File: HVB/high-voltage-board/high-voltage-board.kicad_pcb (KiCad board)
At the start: 2 copper layers, 66 parts, among them J1 Conn_01x23, J10 Conn_01x05, J2 HECS, J3 HV+, J4 HV-, J5 HV+, J6 HV-, J7 Conn_01x02, J9 Bender-LV, Q1 040N03LG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

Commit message: working on layout
Updating traces for RCB and organizing HVB
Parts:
- removed R13: 10k, Resistor_SMD:R_0603_1608Metric_Pad0.98x0.95mm_HandSolder
- C11, C18, C7, R11, R14, R16, R17, R18, R19, R2, U2, U6, U8, U9: moved to B.Cu
- moved R11 135.3 mm to (141.2, 108.7), turned to -90 degrees
- moved R6 133.7 mm to (136.1, 50.3)
- moved C14 128.4 mm to (144.8, 83.3)
- moved Q2 128.2 mm to (147.3, 59.9)
- moved C18 124.4 mm to (145.4, 104.6)
- moved C10 123.6 mm to (145.8, 74.8), turned to 90 degrees
- moved J2 121.4 mm to (68.1, 123.1), turned to 90 degrees
- moved J9 118.0 mm to (78.0, 113.1), turned to -90 degrees
- moved R14 117.2 mm to (145.4, 110.7)
- moved C13 117.0 mm to (144.8, 81.3)
- moved C7 115.9 mm to (143.8, 95.0), turned to -90 degrees
- moved C17 115.8 mm to (149.9, 69.6), turned to 90 degrees
- moved C11 114.6 mm to (143.8, 91.1), turned to 90 degrees
- moved R8 112.2 mm to (144.8, 79.2), turned to 180 degrees
- moved C16 111.6 mm to (151.9, 69.6), turned to 90 degrees
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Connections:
- net /HV+ renamed HV+
- net /HV- renamed HV-
- J1 pad 21: unconnected-(J1-Pad21) -> +5VA
- J1 pad 22: +5V -> unconnected-(J1-Pad22)
- J1 pad 9: /FANOUT2 -> /DCDC_OUT
- J10 pad 1: +3V3 -> A13_SWDIO
- J10 pad 2: A13_SWDIO -> A14_SWCLK
- J10 pad 3: A14_SWCLK -> B3_TRACESWO
- J10 pad 4: B3_TRACESWO -> +3V3
- J2 pad 2: +5V -> +5VA
- J7 pad 1: /TEMP_2 -> /TEMP-
- J7 pad 2: /TEMP_1 -> +3V3
- R12 pad 2: /TEMP_1 -> /TEMP-
- R19 pad 2: +5V -> +3V3
- U5 pad 10: /DC_DC_TRIM_EN -> unconnected-(U5-Pad10)
- U5 pad 13: /TEMP_1 -> unconnected-(U5-Pad13)
- U5 pad 14: /TEMP_2 -> unconnected-(U5-Pad14)
- U5 pad 16: /DC_DC_EN -> unconnected-(U5-Pad16)
- U5 pad 2: /controller/LED1 -> unconnected-(U5-Pad2)
- U5 pad 29: /DC_DC_FAULT -> unconnected-(U5-Pad29)
- U5 pad 3: /controller/LED2 -> unconnected-(U5-Pad3)
- U5 pad 41: unconnected-(U5-Pad41) -> /TEMP-
- U5 pad 42: unconnected-(U5-Pad42) -> /DC_DC_FAULT
- U5 pad 43: unconnected-(U5-Pad43) -> /DC_DC_EN
- U5 pad 45: unconnected-(U5-Pad45) -> /DC_DC_TRIM_EN

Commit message: updating trace layout
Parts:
- moved R1 25.4 mm to (88.9, 53.3), turned to 0 degrees
- moved L1 8.87 mm to (47.8, 57.4), turned to -90 degrees
- moved J5 7.73 mm to (29.8, 43.2)
- moved J3 5.08 mm to (32.5, 73.2)
- moved J4 5.08 mm to (33.0, 93.0)
- moved J6 4.02 mm to (41.7, 105.8)
- moved R15 2.73 mm to (41.1, 57.4), turned to 90 degrees
- moved RV1 2.59 mm to (65.0, 55.4)
- moved C15 1.27 mm to (153.9, 68.3)
- moved C16 1.27 mm to (151.9, 68.3)
- moved C17 1.27 mm to (149.9, 68.3)
- moved C8 1.27 mm to (151.7, 127.8)
- moved C9 1.27 mm to (147.8, 127.8)
- moved D1 1.27 mm to (150.9, 124.5)
- moved D2 1.27 mm to (157.0, 121.7)
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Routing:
- net HV+: track 0.00 -> 125.7 mm
- net /vicor/HV+: track 0.00 -> 29.2 mm
- net /TSAL/HV+: track 0.00 -> 8.96 mm
- net Net-(C19-Pad1): track 0.00 -> 6.83 mm
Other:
- board outline added: 135.9 x 96.5 mm

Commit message: adding traces
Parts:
- R16: moved to F.Cu
- moved R16 12.8 mm to (67.6, 62.2), turned to 0 degrees
- moved RV1 6.76 mm to (59.1, 52.1), turned to -90 degrees
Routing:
- net HV-: track 0.00 -> 42.0 mm
- net /vicor/TRIM_HV: track 0.00 -> 37.4 mm
- added copper zone on B.Cu, net HV-
- added copper zone on F.Cu, net HV-
- added copper zone on F.Cu, net Net-(C19-Pad1)

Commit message: updating hv layout
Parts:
- moved R2 6.72 mm to (100.6, 72.1)
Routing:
- net HV-: track 42.0 -> 106.1 mm
- net Net-(R1-Pad1): track 0.00 -> 30.5 mm
- net /vicor/FAULT_HV: track 0.00 -> 27.0 mm
- net /vicor/EN_HV: track 0.00 -> 22.9 mm
- net /DC_DC_FAULT: track 0.00 -> 3.98 mm
- net Net-(R18-Pad2): track 0.00 -> 3.91 mm
- net Net-(R17-Pad1): track 0.00 -> 3.05 mm
- added copper zone on B.Cu, net Net-(C19-Pad1)
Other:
- outline, holes or cut-outs redrawn
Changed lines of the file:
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@@
   )
   (footprint "Resistor_SMD:R_0603_1608Metric_Pad0.98x0.95mm_HandSolder" (layer "B.Cu")
-    (at 94.5915 69.088)
+    (at 100.584 72.136)
     (descr "Resistor SMD 0603 (1608 Metric), square (rectangular) end terminal, IPC_7351 nominal with elongated pad for handsoldering. (Body size source: IPC-SM-782 page 72, https://www.pcb-3d.com/wordpress/wp-content/uploads/ipc-sm-782a_amendment_1_and_2.pdf), generated with kicad-footprint-generator")
     (tags "resistor handsolder")
@@
   )
   (gr_line (start 161.29 129.54) (end 160.02 129.54) (layer "Edge.Cuts") (width 0.1))
+  (gr_line (start 90.932 104.14) (end 90.932 103.124) (layer "Edge.Cuts") (width 0.1))
+  (gr_arc (start 117.856 39.624) (mid 120.904 36.576) (end 123.952 39.624) (layer "Edge.Cuts") (width 0.1))
+  (gr_line (start 92.456 90.424) (end 90.932 94.488) (layer "Edge.Cuts") (width 0.1))
+  (gr_line (start 92.456 70.612) (end 92.456 68.58) (layer "Edge.Cuts") (width 0.1))
+  (gr_line (start 92.456 85.852) (end 92.456 90.424) (layer "Edge.Cuts") (width 0.1))
+  (gr_line (start 117.856 56.388) (end 117.856 39.624) (layer "Edge.Cuts") (width 0.1))
+  (gr_line (start 87.884 99.568) (end 87.884 104.14) (layer "Edge.Cuts") (width 0.1))
   (gr_line (start 25.4 33.02) (end 158.75 33.02) (layer "Edge.Cuts") (width 0.1))
   (gr_line (start 25.4 38.1) (end 25.4 129.54) (layer "Edge.Cuts") (width 0.1))
+  (gr_arc (start 123.952 62.484) (mid 120.904 65.532) (end 117.856 62.484) (layer "Edge.Cuts") (width 0.1))
+  (gr_arc (start 87.884 67.056) (mid 90.17 64.77) (end 92.456 67.056) (layer "Edge.Cuts") (width 0.1))
+  (gr_line (start 90.932 94.488) (end 90.932 103.124) (layer "Edge.Cuts") (width 0.1))
   (gr_line (start 158.75 33.02) (end 161.29 33.02) (layer "Edge.Cuts") (width 0.1))
   (gr_line (start 25.4 38.1) (end 25.4 33.02) (layer "Edge.Cuts") (width 0.1))
+  (gr_line (start 92.456 67.056) (end 92.456 68.58) (layer "Edge.Cuts") (width 0.1))
   (gr_line (start 161.29 33.02) (end 161.29 129.54) (layer "Edge.Cuts") (width 0.1))
+  (gr_arc (start 90.932 104.14) (mid 89.408 105.664) (end 87.884 104.14) (layer "Edge.Cuts") (width 0.1))
+  (gr_line (start 87.884 67.056) (end 87.884 68.58) (layer "Edge.Cuts") (width 0.1))
+  (gr_line (start 117.856 56.388) (end 117.856 62.484) (layer "Edge.Cuts") (width 0.1))
+  (gr_line (start 87.884 99.568) (end 87.884 68.58) (layer "Edge.Cuts") (width 0.1))
+  (gr_line (start 123.952 39.624) (end 123.952 62.484) (layer "Edge.Cuts") (width 0.1))
   (gr_line (start 25.4 129.54) (end 160.02 129.54) (layer "Edge.Cuts") (width 0.1))
+  (gr_line (start 92.456 70.612) (end 92.456 85.852) (layer "Edge.Cuts") (width 0.1))
+  (dimension (type aligned) (layer "B.SilkS")
+    (pts (xy 87.884 67.056) (xy 92.456 67.056))
+    (height -3.556)
+    (gr_text "4.5720 mm" (at 90.17 62.35) (layer "B.SilkS")
+      (effects (font (size 1 1) (thickness 0.15)))
+    )
+    (format (units 3) (units_format 1) (precision 4))
+    (style (thickness 0.15) (arrow_length 1.27) (text_position_mode 0) (extension_height 0.58642) (extension_offset 0.5) keep_text_aligned)
+  )
+  (dimension (type aligned) (layer "F.SilkS")
+    (pts (xy 117.856 39.624) (xy 123.952 39.624))
+    (height -4.064)
+    (gr_text "6.0960 mm" (at 120.904 34.41) (layer "F.SilkS")
+      (effects (font (size 1 1) (thickness 0.15)))
+    )
+    (format (units 3) (units_format 1) (precision 4))
+    (style (thickness 0.15) (arrow_length 1.27) (text_position_mode 0) (extension_height 0.58642) (extension_offset 0.5) keep_text_aligned)
+  )
   (dimension (type aligned) (layer "Dwgs.User")
     (pts (xy 22.86 137.16) (xy 22.445 36.83))
@@
   (segment (start 41.148 60.454) (end 47.202 60.454) (width 3.6) (layer "F.Cu") (net 12))
   (segment (start 47.202 60.454) (end 47.752 59.904) (width 3.6) (layer "F.Cu") (net 12))
+  (segment (start 85.852 53.34) (end 88.9 53.34) (width 0.36) (layer "B.Cu") (net 30))
+  (segment (start 81.534 74.93) (end 79.756 73.152) (width 0.36) (layer "B.Cu") (net 30))
+  (segment (start 79.756 73.152) (end 79.756 59.436) (width 0.36) (layer "B.Cu") (net 30))
+  (segment (start 84.135 74.93) (end 81.534 74.93) (width 0.36) (layer "B.Cu") (net 30))
+  (segment (start 79.756 59.436) (end 85.852 53.34) (width 0.36) (layer "B.Cu") (net 30))
+  (segment (start 85.75 97.79) (end 83.058 97.79) (width 0.36) (layer "B.Cu") (net 35))
+  (segment (start 83.058 97.79) (end 82.804 97.536) (width 0.36) (layer "B.Cu") (net 35))
+  (segment (start 82.804 99.361) (end 76.91322 99.361) (width 0.36) (layer "B.Cu") (net 36))
+  (segment (start 76.91322 99.361) (end 62.00512 84.4529) (width 0.36) (layer "B.Cu") (net 36))
+  (segment (start 97.536 83.7165) (end 97.4325 83.82) (width 0.36) (layer "B.Cu") (net 38))
+  (segment (start 97.4325 83.82) (end 93.665 83.82) (width 0.36) (layer "B.Cu") (net 38))
+  (segment (start 95.965 97.79) (end 96.012 97.743) (width 0.36) (layer "B.Cu") (net 39))
+  (segment (start 92.05 97.79) (end 95.965 97.79) (width 0.36) (layer "B.Cu") (net 39))
   (segment (start 68.025 52.15) (end 71.12 55.245) (width 0.36) (layer "F.Cu") (net 41))
   (segment (start 71.12 55.245) (end 71.12 72.39) (width 0.36) (layer "F.Cu") (net 41))
@@
   (segment (start 64.12 52.15) (end 68.025 52.15) (width 0.36) (layer "F.Cu") (net 41))
   (segment (start 64.1329 79.3729) (end 62.00512 79.3729) (width 0.36) (layer "F.Cu") (net 41))
+  (segment (start 84.135 83.82) (end 80.772 83.82) (width 0.36) (layer "B.Cu") (net 66))
+  (segment (start 78.8649 81.9129) (end 62.00512 81.9129) (width 0.36) (layer "B.Cu") (net 66))
+  (segment (start 80.772 83.82) (end 78.8649 81.9129) (width 0.36) (layer "B.Cu") (net 66))
   (segment (start 58.42 76.835) (end 57.15 78.105) (width 0.36) (layer "F.Cu") (net 67))
   (segment (start 57.15 90.72806) (end 61.03484 94.6129) (width 0.36) (layer "F.Cu") (net 67))
@@
   (segment (start 68.5 62.23) (end 68.5 72.47) (width 0.36) (layer "F.Cu") (net 67))
   (segment (start 64.135 76.835) (end 58.42 76.835) (width 0.36) (layer "F.Cu") (net 67))
+  (segment (start 72.644 101.092) (end 66.1649 94.6129) (width 0.36) (layer "B.Cu") (net 67))
+  (segment (start 86.36 94.996) (end 86.36 89.916) (width 0.36) (layer "B.Cu") (net 67))
+  (segment (start 86.36 89.916) (end 86.36 73.66) (width 0.36) (layer "B.Cu") (net 67))
+  (segment (start 84.135 87.691) (end 86.36 89.916) (width 0.36) (layer "B.Cu") (net 67))
+  (segment (start 87.376 99.568) (end 85.852 101.092) (width 0.36) (layer "B.Cu") (net 67))
+  (segment (start 87.376 96.012) (end 87.376 99.568) (width 0.36) (layer "B.Cu") (net 67))
+  (segment (start 87.376 96.012) (end 86.614 95.25) (width 0.36) (layer "B.Cu") (net 67))
+  (segment (start 86.36 73.66) (end 85.09 72.39) (width 0.36) (layer "B.Cu") (net 67))
+  (segment (start 85.75 95.25) (end 86.614 95.25) (width 0.36) (layer "B.Cu") (net 67))
+  (segment (start 85.852 101.092) (end 72.644 101.092) (width 0.36) (layer "B.Cu") (net 67))
+  (segment (start 85.09 72.39) (end 84.135 72.39) (width 0.36) (layer "B.Cu") (net 67))
+  (segment (start 84.135 86.36) (end 84.135 87.691) (width 0.36) (layer "B.Cu") (net 67))
+  (segment (start 66.1649 94.6129) (end 61.03484 94.6129) (width 0.36) (layer "B.Cu") (net 67))
+  (segment (start 86.614 95.25) (end 86.36 94.996) (width 0.36) (layer "B.Cu") (net 67))
   (segment (start 29.82 43.18) (end 29.82 70.46) (width 3.6) (layer "F.Cu") (net 68))
   (segment (start 91.62 38.81952) (end 91.62 44.45) (width 3.6) (layer "F.Cu") (net 68))
@@
   (segment (start 41.698 54.904) (end 41.148 54.354) (width 3.6) (layer "F.Cu") (net 74))
   (segment (start 47.752 54.904) (end 41.698 54.904) (width 3.6) (layer "F.Cu") (net 74))
-  (zone (net 12) (net_name "Net-(C19-Pad1)") (layer "F.Cu") (hatch edge 0.508)
+  (zone (net 12) (net_name "Net-(C19-Pad1)") (layers F&B.Cu) (hatch edge 0.508)
     (priority 1)
     (connect_pads (clearance 0.508))

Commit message: working on layout
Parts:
- moved J9 9.91 mm to (68.1, 113.4)
- moved J2 8.66 mm to (76.7, 123.4)
- moved D1 1.55 mm to (149.4, 124.2), turned to 180 degrees
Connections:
- D1 pad 2: VDD -> +12V
- J1 pad 1: +12V -> /DCDC_OUT
- J1 pad 10: +12V -> +5VA
- J1 pad 11: GND -> unconnected-(J1-Pad11)
- J1 pad 12: /CAN- -> GND
- J1 pad 13: /CAN+ -> +12V
- J1 pad 14: /DCDC_OUT -> /CAN+
- J1 pad 15: /CAN- -> /CAN+
- J1 pad 16: /CAN+ -> /HECS_AN1
- J1 pad 18: /HECS_AN2 -> /IMD_OK
- J1 pad 19: /HECS_AN1 -> unconnected-(J1-Pad19)
- J1 pad 2: /TSAL_GND -> /DCDC_OUT
- J1 pad 20: /IMD_OK -> +12V
- J1 pad 21: +5VA -> GND
- J1 pad 22: unconnected-(J1-Pad22) -> /CAN-
- J1 pad 23: unconnected-(J1-Pad23) -> /CAN-
- J1 pad 3: +12V -> /DCDC_OUT
- J1 pad 4: GND -> /DCDC_OUT
- J1 pad 6: GND -> +12V
- J1 pad 7: /DCDC_OUT -> +12V
- J1 pad 8: /DCDC_OUT -> /TSAL_GND
- J1 pad 9: /DCDC_OUT -> /HECS_AN2
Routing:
- net +12V: track 0.00 -> 101.4 mm
- net /IMD_OK: track 0.00 -> 44.0 mm
- net +5VA: track 0.00 -> 36.9 mm
- net /HECS_AN2: track 0.00 -> 33.8 mm
- net /HECS_AN3: track 0.00 -> 31.6 mm
- net /HECS_AN1: track 0.00 -> 26.4 mm
- added copper zone on B.Cu, net GND
- added copper zone on F.Cu, net GND

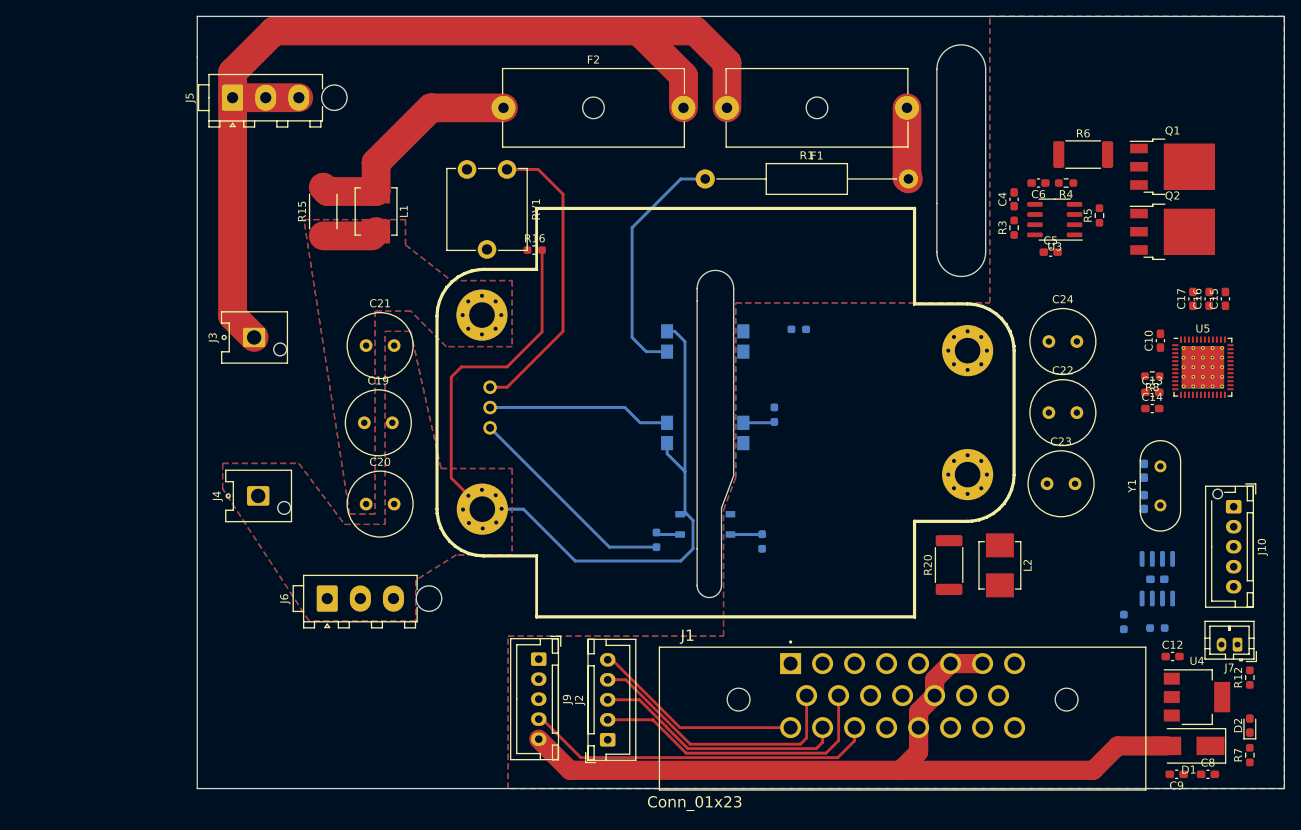
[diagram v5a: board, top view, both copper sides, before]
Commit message: almost done with layout
HV layout almost done. Tracing
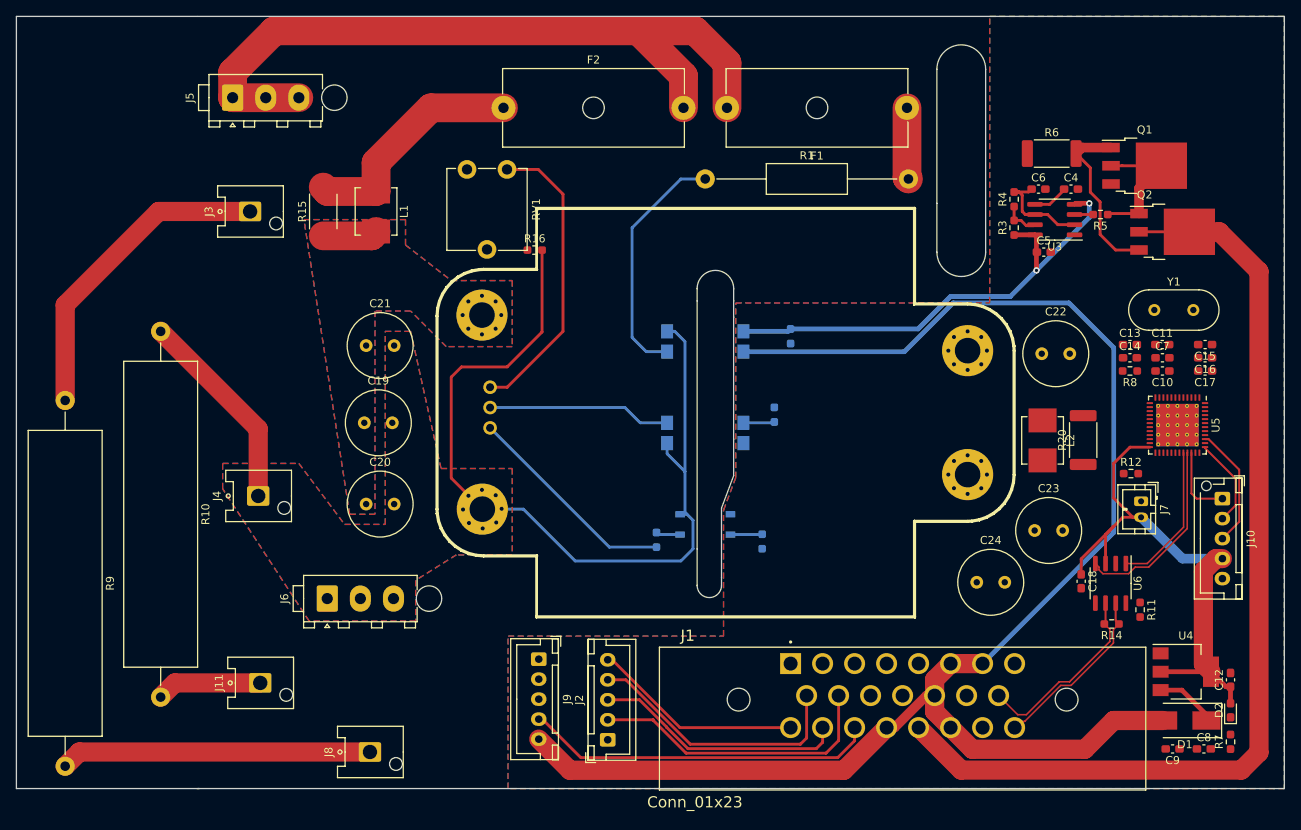
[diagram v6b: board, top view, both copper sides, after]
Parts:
- added J11: HV-, Connector_Hirose:Hirose_DF63M-1P-3.96DSA_1x01_P3.96mm_Vertical, F.Cu at (33.3, 116.3)
- added J8: HV+, Connector_Hirose:Hirose_DF63M-1P-3.96DSA_1x01_P3.96mm_Vertical, F.Cu at (47.0, 125.0)
- added R10: R, Resistor_THT:R_Axial_Power_L38.0mm_W9.0mm_P45.72mm, F.Cu at (20.8, 72.4)
- added R9: R, Resistor_THT:R_Axial_Power_L38.0mm_W9.0mm_P45.72mm, F.Cu at (8.89, 81.0)
- C11, C18, C7, R11, R14, U6: moved to F.Cu
- moved C24 31.4 mm to (122.8, 103.8)
- moved R12 29.5 mm to (142.1, 90.2), turned to 0 degrees
- moved Y1 24.4 mm to (145.0, 69.7), turned to 0 degrees
- moved R20 22.9 mm to (136.1, 86.0)
- moved J7 21.6 mm to (143.4, 93.6), turned to -90 degrees
- moved C7 18.2 mm to (146.1, 75.7), turned to 0 degrees
- moved L2 16.5 mm to (131.1, 86.0)
- moved C11 15.9 mm to (146.0, 74.0), turned to 0 degrees
- moved J3 15.8 mm to (32.0, 57.4)
- moved C18 9.53 mm to (135.9, 103.6), turned to -90 degrees
- moved C17 9.14 mm to (151.4, 77.3), turned to 180 degrees
- moved U5 7.91 mm to (147.9, 84.1), turned to -90 degrees
- moved C12 7.81 mm to (154.6, 116.0), turned to 90 degrees
- moved C22 7.42 mm to (131.0, 75.2)
- moved C16 7.38 mm to (151.4, 75.7), turned to 180 degrees
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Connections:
- net /controller/CAN_RX_N renamed /controller/CAN_X_N
- net /controller/CAN_TX_P renamed /controller/CAN_X_P
- J1 pad 11: unconnected-(J1-Pad11) -> GND
- J1 pad 14: /CAN+ -> /CAN-
- J1 pad 15: /CAN+ -> /CAN-
- J1 pad 19: unconnected-(J1-Pad19) -> +12V
- J1 pad 20: +12V -> /TSAL_GND
- J1 pad 21: GND -> +12V
- J1 pad 22: /CAN- -> /CAN+
- J1 pad 23: /CAN- -> /CAN+
- J1 pad 8: /TSAL_GND -> unconnected-(J1-Pad8)
- U5 pad 10: unconnected-(U5-Pad10) -> /DC_DC_TRIM_EN
- U5 pad 11: unconnected-(U5-Pad11) -> /DC_DC_EN
- U5 pad 12: unconnected-(U5-Pad12) -> /DC_DC_FAULT
- U5 pad 29: unconnected-(U5-Pad29) -> /TEMP-
- U5 pad 38: A15 -> unconnected-(U5-Pad38)
- U5 pad 41: /TEMP- -> unconnected-(U5-Pad41)
- U5 pad 42: /DC_DC_FAULT -> unconnected-(U5-Pad42)
- U5 pad 43: /DC_DC_EN -> unconnected-(U5-Pad43)
- U5 pad 45: /DC_DC_TRIM_EN -> unconnected-(U5-Pad45)
- U7 pad 8: Net-(C22-Pad1) -> GND
- U7 pad 9: GND -> Net-(C22-Pad1)
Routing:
- net /TSAL_GND: track 0.00 -> 122.8 mm
- net +12V: track 101.4 -> 195.2 mm
- net +3V3: track 0.00 -> 70.5 mm
- net VCC: track 0.00 -> 59.9 mm, vias 0 -> 2
- net Net-(J8-Pad1): track 0.00 -> 38.8 mm
- net HV-: track 106.1 -> 131.7 mm
- net /controller/CAN_X_N: track 0.00 -> 24.0 mm
- net /CAN-: track 0.00 -> 23.8 mm
- net /CAN+: track 0.00 -> 22.2 mm
- net Net-(Q1-Pad1): track 0.00 -> 21.7 mm
- net /controller/CAN_X_P: track 0.00 -> 18.4 mm
- net Net-(Q1-Pad2): track 0.00 -> 17.4 mm
- net B3_TRACESWO: track 0.00 -> 15.3 mm
- net Net-(J11-Pad1): track 0.00 -> 13.2 mm
- net /TSAL/pass: track 0.00 -> 12.8 mm
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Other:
- board size 135.9 x 96.5 mm -> 158.5 x 96.5 mm
